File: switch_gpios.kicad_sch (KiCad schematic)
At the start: 52 parts

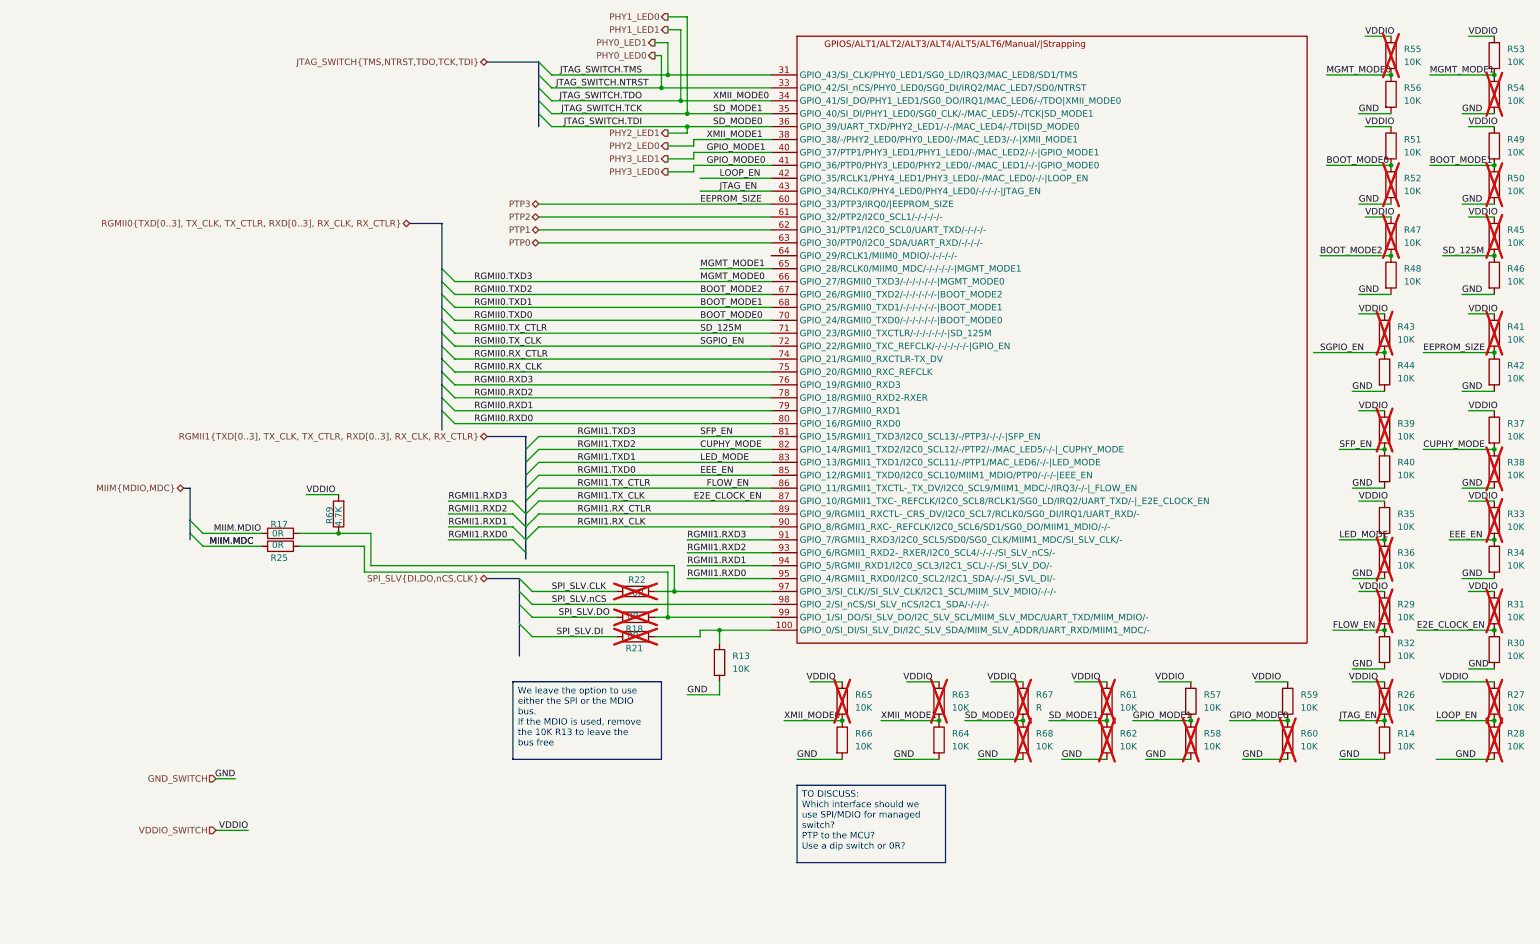
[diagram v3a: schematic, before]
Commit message: switch: finished 1st version
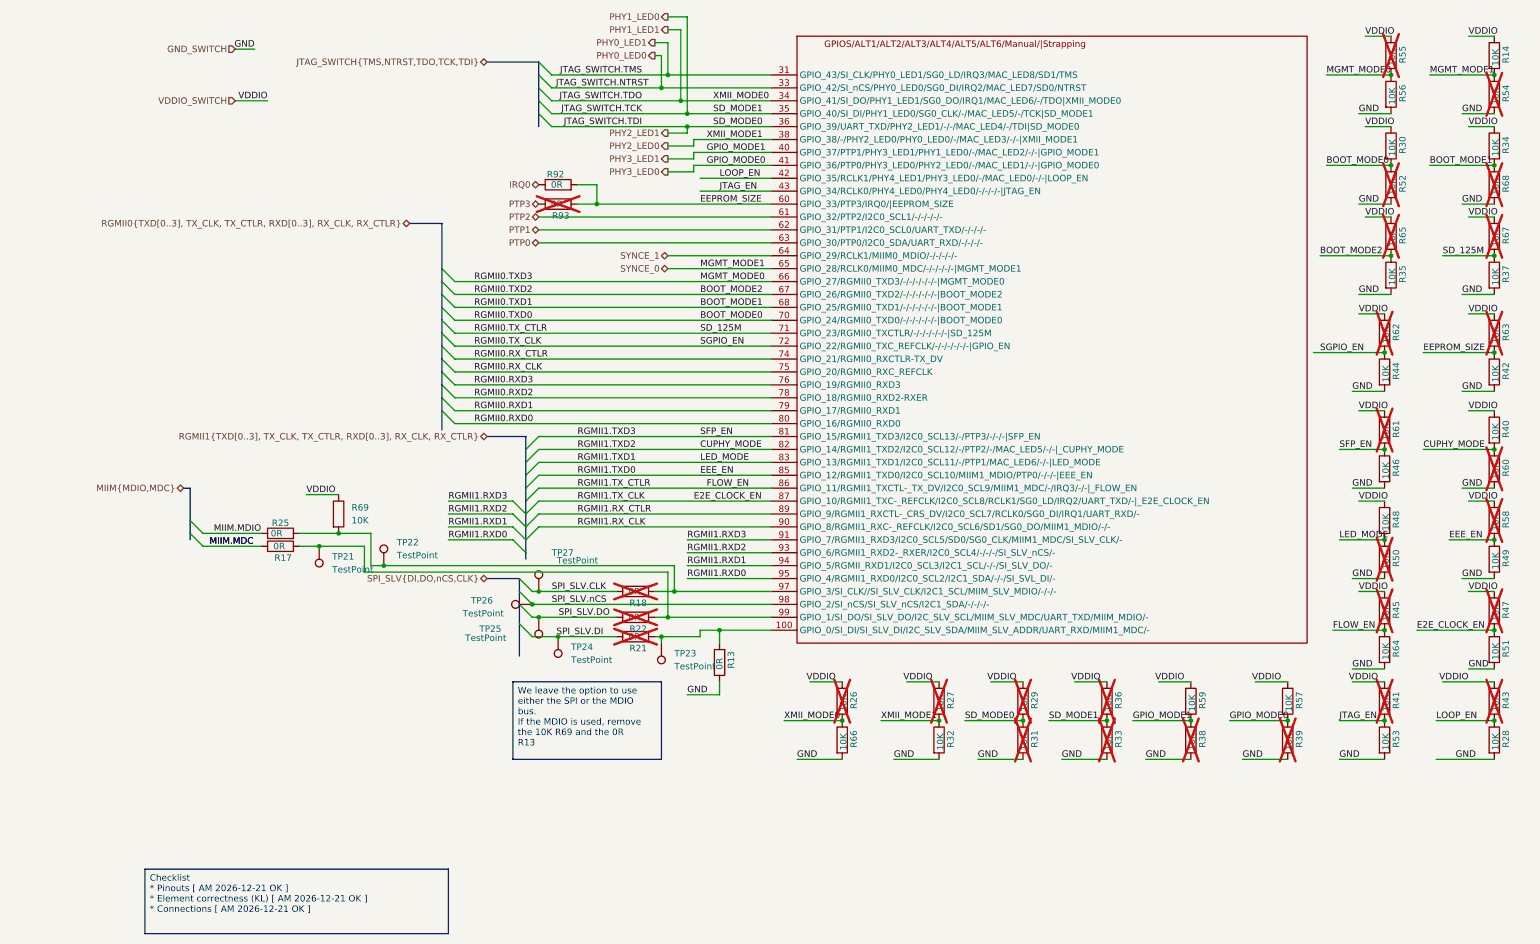
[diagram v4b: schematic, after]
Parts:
- removed R13, R14, R26, R27, R28, R29, R30, R31, R32, R33, R34, R35, R36, R37, R38, R39, R40, R41, R42, R43, R44, R45, R46, R47, R48, R49, R50, R51, R52, R53, R54, R55, R56, R57, R58, R59, R60, R61, R62, R63, R64, R65, R66, R68: 10K, symbol Device:R
- removed R17, R18, R21, R22, R25: 0R, symbol Device:R
- removed R67: R, symbol Device:R
- removed R69: 4.7K, symbol Device:R
- added R13, R17, R18, R21, R22, R25, R92, R93: 0R, KL:R_0603, symbol KL_R:R_0R_250mW_0.5_0603
- added R14, R26, R27, R28, R29, R30, R31, R32, R33, R34, R35, R36, R37, R38, R39, R40, R41, R42, R43, R44, R45, R46, R47, R48, R49, R50, R51, R52, R53, R54, R55, R56, R57, R58, R59, R60, R61, R62, R63, R64, R65, R66, R67, R68, R69: 10K, KL:R_0603, symbol KL_R:R_10K_100mW_5_0603
- added TP21, TP22, TP23, TP24, TP25, TP26, TP27: TestPoint, symbol Connector:TestPoint
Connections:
- net BOOT_MODE0: now also R30.2, R52.1
- net BOOT_MODE1: now also R34.2, R68.1
- net BOOT_MODE2: now also R35.1, R65.2
- net CUPHY_MODE: now also R40.2, R60.1
- net E2E_CLOCK_EN: now also R47.2, R51.1
- net EEE_EN: now also R49.1, R58.2
- net FLOW_EN: now also R45.2, R64.1
- net GND_SWITCH: now also R13.1, R28.2, R31.2, R32.2, R33.2, R35.2, R37.2, R38.2, R39.2, R42.2, R44.2, R46.2, R49.2, R50.2, R51.2, R52.2, R53.2, R54.2, R56.2, R60.2, R64.2, R66.2, R68.2
- net JTAG_EN: now also R41.2, R53.1
- net LED_MODE: now also R48.2, R50.1
- net LOOP_EN: now also R28.1, R43.2
- net MGMT_MODE0: now also R55.2, R56.1
- net MIIM.MDC: now also R17.1
- net MIIM.MDIO: now also R25.1
- net PHY1_LED0: now also R33.1, R36.2
- net PHY1_LED1: now also R26.2, R66.1
- net PHY2_LED0: now also R27.2, R32.1
- net PHY2_LED1: now also R29.2, R31.1
- net PHY3_LED0: now also R39.1, R57.2
- net PHY3_LED1: now also R38.1, R59.2
- net PTP3: now also R93.1; no longer U1.60 (GPIO_33/PTP3/IRQ0/|EEPROM_SIZE)
- net RGMII0.TX_CLK: now also R44.1, R62.2
- net RGMII0.TX_CTLR: now also R37.1, R67.2
- net RGMII1.TXD3: now also R46.1, R61.2
- net SPI_SLV.CLK: now also R18.1, TP27.1
- net SPI_SLV.DI: now also R21.1, TP24.1
- net SPI_SLV.DO: now also R22.1, TP25.1
- net SPI_SLV.nCS: now also TP26.1
- net VDDIO_SWITCH: now also R14.1, R26.1, R27.1, R29.1, R30.1, R34.1, R36.1, R40.1, R41.1, R43.1, R45.1, R47.1, R48.1, R55.1, R57.1, R58.1, R59.1, R61.1, R62.1, R63.1, R65.1, R67.1, R69.1
- net at U1.100 (GPIO_0/SI_DI/SI_SLV_DI/I2C_SLV_SDA/MIIM_SLV_ADDR/UART_RXD/MIIM1_MDC/-): now also R13.2, R21.2, TP23.1
- net at U1.97 (GPIO_3/SI_CLK//SI_SLV_CLK/I2C1_SCL/MIIM_SLV_MDIO/-/-/-): now also R18.2, R25.2, R69.2, TP22.1
- net at U1.99 (GPIO_1/SI_DO/SI_SLV_DO/I2C_SLV_SCL/MIIM_SLV_MDC/UART_TXD/MIIM_MDIO/-): now also R17.2, R22.2, TP21.1
- net SYNCE_1: now reaches U1.64 (GPIO_29/RCLK1/MIIM0_MDIO/-/-/-/-/-)
- net MGMT_MODE1 renamed SYNCE_0
- net SYNCE_0: now also R14.2, R54.1
- new net EEPROM_SIZE: R42.1, R63.2, R92.2, R93.2, U1.60 (GPIO_33/PTP3/IRQ0/|EEPROM_SIZE)
- new net IRQ0: R92.1
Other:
- company: (none) -> Kebag-Logic <contac@kebag-logic.com>

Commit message: minor footprint fixing
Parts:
- U1: footprint Package_QFP:TQFP-128_14x14mm_P0.4mm -> KL:TQFP-128_14x14mm_P0.4mm_with_EPAD; symbol lan9645xF:lan9645xF_128_TQFP -> KL_IC_LAN9645xF:lan9645xF_128_TQFP; Digikey (none) -> 150-LAN96455FT-I/8MWTR-ND; Mouser (none) -> 579-LAN96455FTI8MW; manf# LAN96455F-I/8MW -> (none)
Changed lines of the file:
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@@
 	)
 	(symbol
-		(lib_id "lan9645xF:lan9645xF_128_TQFP")
+		(lib_id "KL_IC_LAN9645xF:lan9645xF_128_TQFP")
 		(at 142.24 34.29 0)
 		(unit 2)
@@
 			)
 		)
-		(property "Footprint" "Package_QFP:TQFP-128_14x14mm_P0.4mm"
-			(at 142.24 34.29 0)
+		(property "Footprint" "KL:TQFP-128_14x14mm_P0.4mm_with_EPAD"
+			(at 155.956 28.448 0)
 			(effects
 				(font
@@
 			)
 		)
-		(property "manf#" "LAN96455F-I/8MW"
+		(property "Mouser" "579-LAN96455FTI8MW "
+			(at 155.194 26.162 0)
+			(effects
+				(font
+					(size 1.27 1.27)
+				)
+				(hide yes)
+			)
+		)
+		(property "Digikey" "150-LAN96455FT-I/8MWTR-ND"
 			(at 142.24 34.29 0)
 			(effects
+				(font
+					(size 1.27 1.27)
+				)
+				(hide yes)
+			)
+		)
+		(property "LSCS" ""
+			(at 142.24 34.29 0)
+			(effects

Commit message: This commit intends to fix multiple issues:
 - 1.1 -> 1.15 v buck rails
 - Revision consistently using Rev. A
 - Issue with the Switch symbol when moving library
 - Adding new footprint and symbol for 2.54mm Headers
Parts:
- U1: footprint KL:TQFP-128_14x14mm_P0.4mm_with_EPAD -> Package_QFP:TQFP-128_14x14mm_P0.4mm; Digikey 150-LAN96455FT-I/8MWTR-ND -> (none); Mouser 579-LAN96455FTI8MW -> (none); manf# (none) -> LAN96455F-I/8MW

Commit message: fixing issue related to symbol changes, and updating components
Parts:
- R13, R14, R17, R18, R21, R22, R25, R26, R27, R28, R29, R30, R31, R32, R33, R34, R35, R36, R37, R38, R39, R40, R41, R42, R43, R44, R45, R46, R47, R48, R49, R50, R51, R52, R53, R54, R55, R56, R57, R58, R59, R60, R61, R62, R63, R64, R65, R66, R67, R68, R69, R92, R93: footprint KL:R_0603 -> KL_Footprints:C_0603
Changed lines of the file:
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@@
 			)
 		)
-		(property "Footprint" "KL:R_0603"
+		(property "Footprint" "KL_Footprints:C_0603"
 			(at 149.352 156.21 90)
 			(effects
@@
 			)
 		)
-		(property "Footprint" "KL:R_0603"
+		(property "Footprint" "KL_Footprints:C_0603"
 			(at 277.622 21.59 90)
 			(effects
@@
 			)
 		)
-		(property "Footprint" "KL:R_0603"
+		(property "Footprint" "KL_Footprints:C_0603"
 			(at 277.622 83.82 90)
 			(effects
@@
 			)
 		)
-		(property "Footprint" "KL:R_0603"
+		(property "Footprint" "KL_Footprints:C_0603"
 			(at 95.25 48.768 90)
 			(effects
@@
 			)
 		)
-		(property "Footprint" "KL:R_0603"
+		(property "Footprint" "KL_Footprints:C_0603"
 			(at 168.402 148.59 90)
 			(effects
@@
 			)
 		)
-		(property "Footprint" "KL:R_0603"
+		(property "Footprint" "KL_Footprints:C_0603"
 			(at 149.352 148.59 90)
 			(effects
@@
 			)
 		)
-		(property "Footprint" "KL:R_0603"
+		(property "Footprint" "KL_Footprints:C_0603"
 			(at 217.932 156.21 90)
 			(effects
@@
 			)
 		)
-		(property "Footprint" "KL:R_0603"
+		(property "Footprint" "KL_Footprints:C_0603"
 			(at 40.64 119.888 90)
 			(effects
@@
 			)
 		)
-		(property "Footprint" "KL:R_0603"
+		(property "Footprint" "KL_Footprints:C_0603"
 			(at 257.302 46.99 90)
 			(effects
@@
 			)
 		)
-		(property "Footprint" "KL:R_0603"
+		(property "Footprint" "KL_Footprints:C_0603"
 			(at 277.622 29.21 90)
 			(effects
@@
 			)
 		)
-		(property "Footprint" "KL:R_0603"
+		(property "Footprint" "KL_Footprints:C_0603"
 			(at 110.49 128.778 90)
 			(effects
@@
 			)
 		)
-		(property "Footprint" "KL:R_0603"
+		(property "Footprint" "KL_Footprints:C_0603"
 			(at 168.402 156.21 90)
 			(effects
@@
 			)
 		)
-		(property "Footprint" "KL:R_0603"
+		(property "Footprint" "KL_Footprints:C_0603"
 			(at 217.932 148.59 90)
 			(effects
@@
 			)
 		)
-		(property "Footprint" "KL:R_0603"
+		(property "Footprint" "KL_Footprints:C_0603"
 			(at 40.64 117.348 90)
 			(effects
@@
 			)
 		)
-		(property "Footprint" "KL:R_0603"
+		(property "Footprint" "KL_Footprints:C_0603"
 			(at 95.25 52.578 90)
 			(effects
@@
 			)
 		)
-		(property "Footprint" "KL:R_0603"
+		(property "Footprint" "KL_Footprints:C_0603"
 			(at 256.032 156.21 90)
 			(effects
@@
 			)
 		)
-		(property "Footprint" "KL:R_0603"
+		(property "Footprint" "KL_Footprints:C_0603"
 			(at 184.912 148.59 90)
 			(effects
@@
 			)
 		)
-		(property "Footprint" "KL:R_0603"
+		(property "Footprint" "KL_Footprints:C_0603"
 			(at 277.622 120.65 90)
 			(effects
@@
 			)
 		)
-		(property "Footprint" "KL:R_0603"
+		(property "Footprint" "KL_Footprints:C_0603"
 			(at 236.982 156.21 90)
 			(effects
@@
 			)
 		)
-		(property "Footprint" "KL:R_0603"
+		(property "Footprint" "KL_Footprints:C_0603"
 			(at 277.622 95.25 90)
 			(effects
@@
 			)
 		)
-		(property "Footprint" "KL:R_0603"
+		(property "Footprint" "KL_Footprints:C_0603"
 			(at 257.302 57.15 90)
 			(effects
@@
 			)
 		)
-		(property "Footprint" "KL:R_0603"
+		(property "Footprint" "KL_Footprints:C_0603"
 			(at 256.032 130.81 90)
 			(effects
@@
 			)
 		)
-		(property "Footprint" "KL:R_0603"
+		(property "Footprint" "KL_Footprints:C_0603"
 			(at 277.622 39.37 90)
 			(effects
@@
 			)
 		)
-		(property "Footprint" "KL:R_0603"
+		(property "Footprint" "KL_Footprints:C_0603"
 			(at 257.302 64.77 90)
 			(effects
@@
 			)
 		)
-		(property "Footprint" "KL:R_0603"
+		(property "Footprint" "KL_Footprints:C_0603"
 			(at 277.622 76.2 90)
 			(effects
@@
 			)
 		)
-		(property "Footprint" "KL:R_0603"
+		(property "Footprint" "KL_Footprints:C_0603"
 			(at 50.292 111.76 90)
 			(effects
@@
 			)
 		)
-		(property "Footprint" "KL:R_0603"
+		(property "Footprint" "KL_Footprints:C_0603"
 			(at 256.032 113.03 90)
 			(effects
@@
 			)
 		)
-		(property "Footprint" "KL:R_0603"
+		(property "Footprint" "KL_Footprints:C_0603"
 			(at 277.622 46.99 90)
 			(effects
@@
 			)
 		)
-		(property "Footprint" "KL:R_0603"
+		(property "Footprint" "KL_Footprints:C_0603"
 			(at 257.302 39.37 90)
 			(effects
@@
 			)
 		)
-		(property "Footprint" "KL:R_0603"
+		(property "Footprint" "KL_Footprints:C_0603"
 			(at 256.032 138.43 90)
 			(effects
@@
 			)
 		)
-		(property "Footprint" "KL:R_0603"
+		(property "Footprint" "KL_Footprints:C_0603"
 			(at 128.778 140.97 90)
 			(effects
@@
 			)
 		)
-		(property "Footprint" "KL:R_0603"
+		(property "Footprint" "KL_Footprints:C_0603"
 			(at 110.49 133.858 90)
 			(effects
@@
 			)
 		)
-		(property "Footprint" "KL:R_0603"
+		(property "Footprint" "KL_Footprints:C_0603"
 			(at 256.032 120.65 90)
 			(effects
@@
 			)
 		)
-		(property "Footprint" "KL:R_0603"
+		(property "Footprint" "KL_Footprints:C_0603"
 			(at 277.622 64.77 90)
 			(effects
@@
 			)
 		)
-		(property "Footprint" "KL:R_0603"
+		(property "Footprint" "KL_Footprints:C_0603"
 			(at 277.622 113.03 90)
 			(effects
@@
 			)
 		)
-		(property "Footprint" "KL:R_0603"
+		(property "Footprint" "KL_Footprints:C_0603"
 			(at 257.302 29.21 90)
 			(effects
@@
 			)
 		)
-		(property "Footprint" "KL:R_0603"
+		(property "Footprint" "KL_Footprints:C_0603"
 			(at 236.982 148.59 90)
 			(effects
@@
 			)
 		)
-		(property "Footprint" "KL:R_0603"
+		(property "Footprint" "KL_Footprints:C_0603"
 			(at 277.622 102.87 90)
 			(effects
@@
 			)
 		)
-		(property "Footprint" "KL:R_0603"
+		(property "Footprint" "KL_Footprints:C_0603"
 			(at 110.49 137.668 90)
 			(effects
@@
 			)
 		)
-		(property "Footprint" "KL:R_0603"
+		(property "Footprint" "KL_Footprints:C_0603"
 			(at 277.622 138.43 90)
 			(effects
@@
 			)
 		)
-		(property "Footprint" "KL:R_0603"
+		(property "Footprint" "KL_Footprints:C_0603"
 			(at 257.302 21.59 90)
 			(effects
@@
 			)
 		)
-		(property "Footprint" "KL:R_0603"
+		(property "Footprint" "KL_Footprints:C_0603"
 			(at 184.912 156.21 90)
 			(effects
@@
 			)
 		)
-		(property "Footprint" "KL:R_0603"
+		(property "Footprint" "KL_Footprints:C_0603"
 			(at 201.422 148.59 90)
 			(effects
@@
 			)
 		)
-		(property "Footprint" "KL:R_0603"
+		(property "Footprint" "KL_Footprints:C_0603"
 			(at 277.622 130.81 90)
 			(effects
@@
 			)
 		)
-		(property "Footprint" "KL:R_0603"
+		(property "Footprint" "KL_Footprints:C_0603"
 			(at 256.032 148.59 90)
 			(effects
@@
 			)
 		)
-		(property "Footprint" "KL:R_0603"
+		(property "Footprint" "KL_Footprints:C_0603"
 			(at 277.622 156.21 90)
 			(effects
@@
 			)
 		)
-		(property "Footprint" "KL:R_0603"
+		(property "Footprint" "KL_Footprints:C_0603"
 			(at 256.032 102.87 90)
 			(effects
@@
 			)
 		)
-		(property "Footprint" "KL:R_0603"
+		(property "Footprint" "KL_Footprints:C_0603"
 			(at 277.622 57.15 90)
 			(effects
@@
 			)
 		)
-		(property "Footprint" "KL:R_0603"
+		(property "Footprint" "KL_Footprints:C_0603"
 			(at 256.032 95.25 90)
 			(effects
@@
 			)
 		)
-		(property "Footprint" "KL:R_0603"
+		(property "Footprint" "KL_Footprints:C_0603"
 			(at 256.032 76.2 90)
 			(effects
@@
 			)
 		)
-		(property "Footprint" "KL:R_0603"
+		(property "Footprint" "KL_Footprints:C_0603"
 			(at 201.422 156.21 90)
 			(effects
@@
 			)
 		)
-		(property "Footprint" "KL:R_0603"
+		(property "Footprint" "KL_Footprints:C_0603"
 			(at 256.032 83.82 90)
 			(effects
@@
 			)
 		)
-		(property "Footprint" "KL:R_0603"
+		(property "Footprint" "KL_Footprints:C_0603"
 			(at 277.622 148.59 90)
 			(effects
